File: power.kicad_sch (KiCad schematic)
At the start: 37 parts, among them J1 +5V SUPPLY, SW1 RESET, U1 NS32201, U19 74AHC32, U2 LM3671, U3 NS32016, U4 NS32082, U5 NS32202, U6 74AHC08, Y1 12.00000MHz

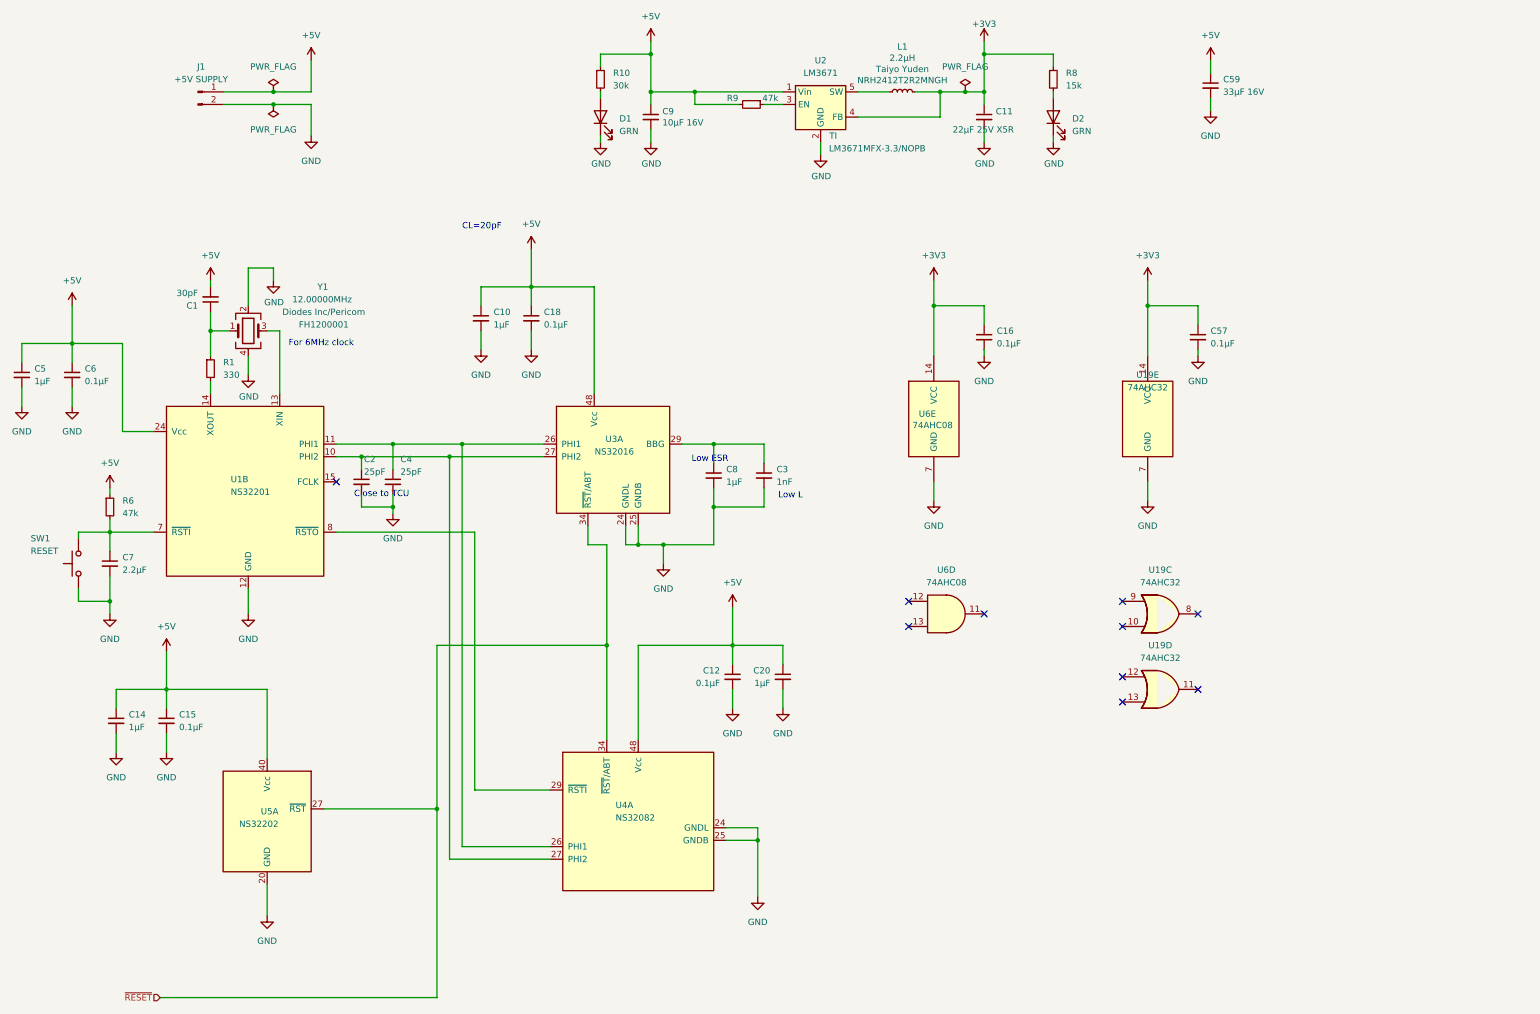
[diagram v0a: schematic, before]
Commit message: Rework RESET/RST: see Changelist
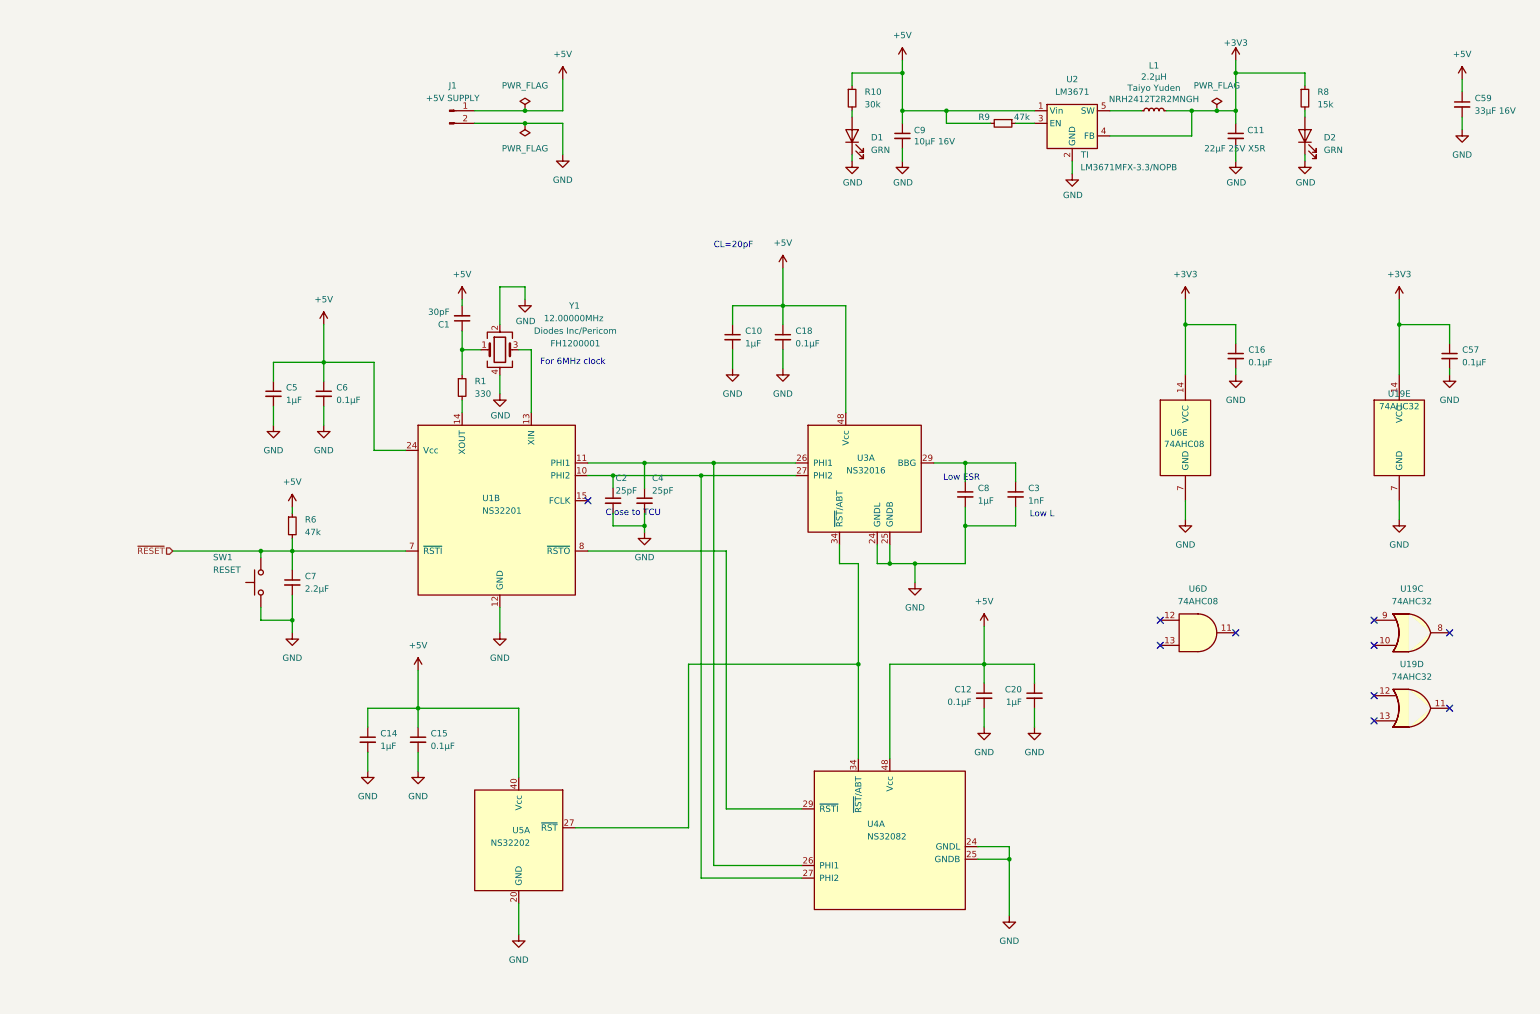
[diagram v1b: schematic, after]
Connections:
- net ~{RESET}: now also C7.1, R6.2, SW1.1, U1.7 (~{RSTI}); no longer U3.34 (~{RST}/ABT), U4.34 (~{RST}/ABT), U5.27 (~{RST})
- new net: U3.34 (~{RST}/ABT), U4.34 (~{RST}/ABT), U5.27 (~{RST})
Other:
- moved on the sheet: C1, C10, C11, C12, C14, C15, C16, C18, C2, C20, C3, C4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

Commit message: fix reset timing, should be 100us, not 100ms...
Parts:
- C7: value 2.2µF -> 0.1µF; footprint Capacitor_SMD:C_0603_1608Metric -> Capacitor_SMD:C_0402_1005Metric
- R6: value 47k -> 1k
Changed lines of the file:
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@@
 			)
 		)
-		(property "Value" "47k"
+		(property "Value" "1k"
 			(at 87.63 137.1599 0)
 			(effects
@@
 			)
 		)
-		(property "Value" "2.2µF"
+		(property "Value" "0.1µF"
 			(at 87.63 148.5962 0)
 			(effects
@@
 			)
 		)
-		(property "Footprint" "Capacitor_SMD:C_0603_1608Metric"
+		(property "Footprint" "Capacitor_SMD:C_0402_1005Metric"
 			(at 85.09 147.32 0)
 			(effects
